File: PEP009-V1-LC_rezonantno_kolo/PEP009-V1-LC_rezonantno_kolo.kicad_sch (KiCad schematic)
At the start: 13 parts, among them J1 Screw_Terminal_01x02

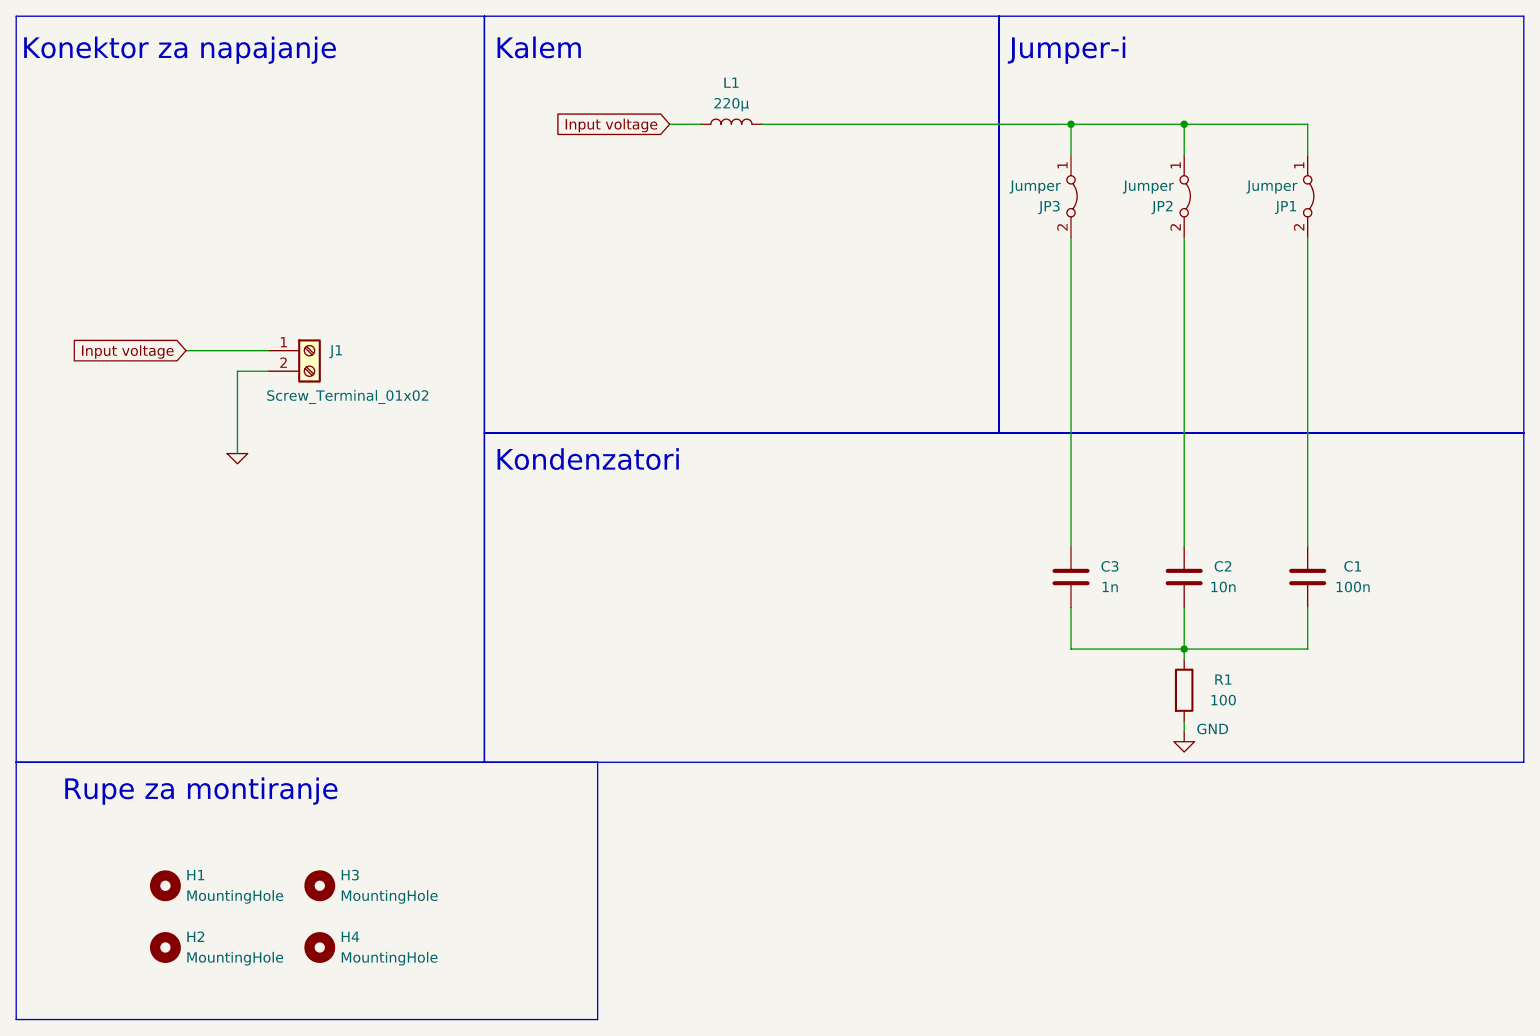
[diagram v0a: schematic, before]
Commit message: PEP006 and PEP009 update.
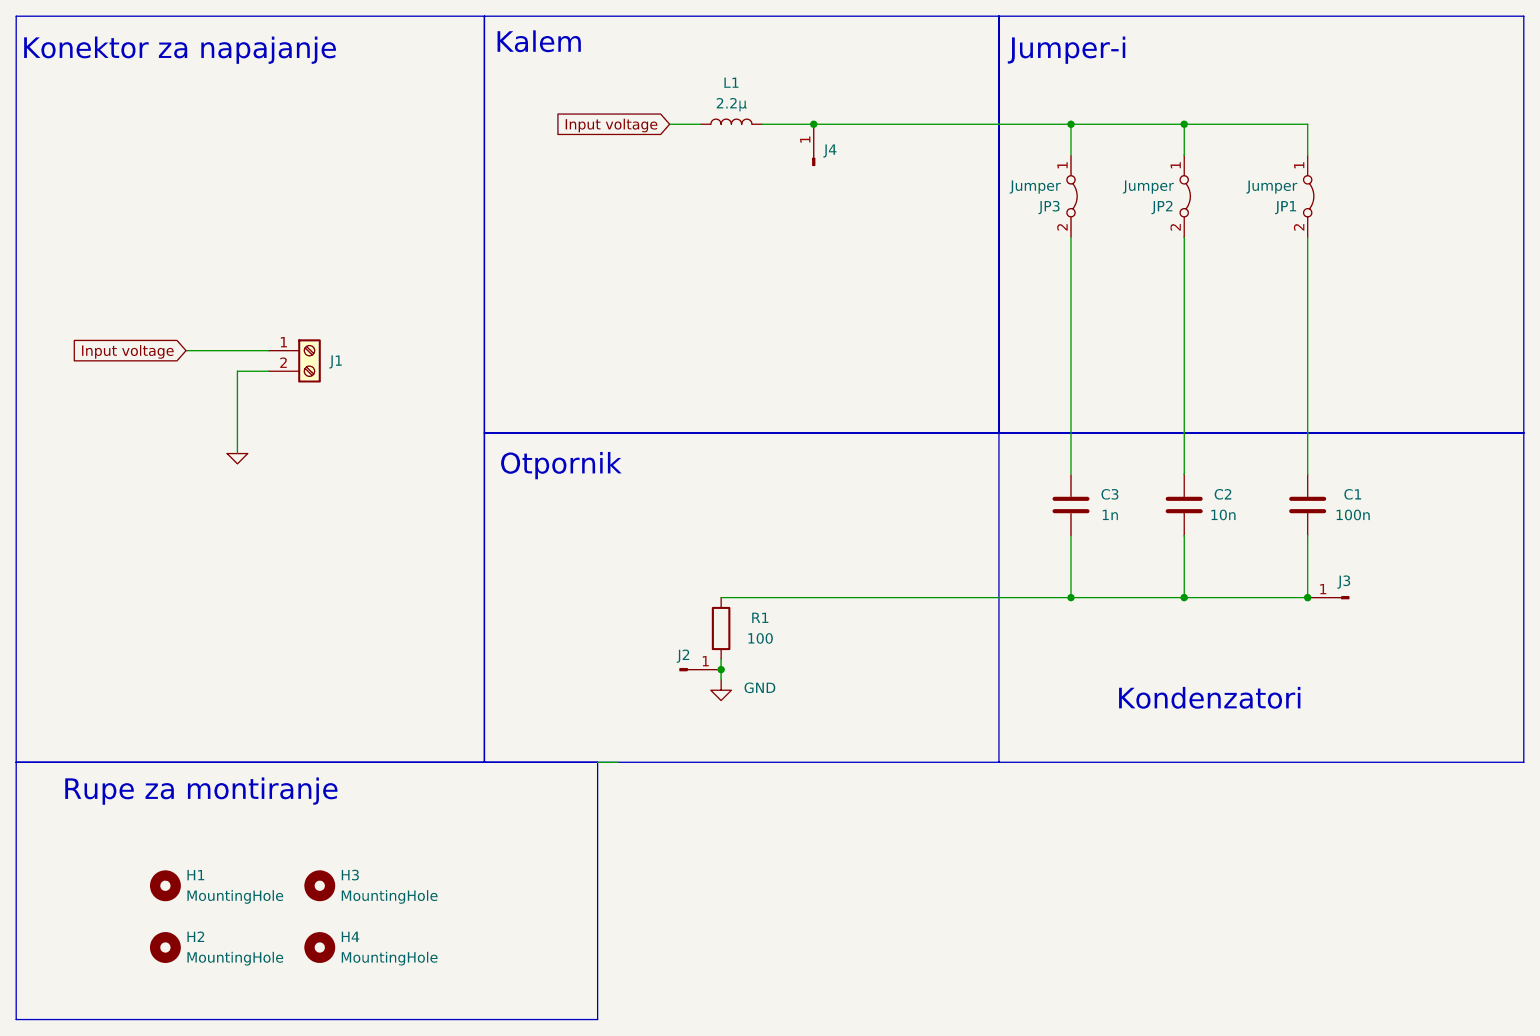
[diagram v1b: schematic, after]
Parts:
- added J2, J3, J4: Conn_01x01_Pin, Connector_PinHeader_2.54mm:PinHeader_1x01_P2.54mm_Vertical, symbol Connector:Conn_01x01_Pin
- C1: footprint Capacitor_SMD:C_1808_4520Metric -> Capacitor_SMD:C_1206_3216Metric; LCSC (none) -> C24497
- C2: footprint Capacitor_SMD:C_1808_4520Metric -> Capacitor_SMD:C_1206_3216Metric; LCSC (none) -> C1846
- C3: footprint Capacitor_SMD:C_1808_4520Metric -> Capacitor_SMD:C_1206_3216Metric; LCSC (none) -> C9196
- L1: value 220µ -> 2.2µ; footprint Inductor_SMD:L_12x12mm_H4.5mm -> Inductor_SMD:L_0805_2012Metric; LCSC (none) -> C55755
- R1: LCSC (none) -> C17901
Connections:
- net GND: now also J2.1 (Pin_1)
- net at C1.2, C2.2, C3.2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: now also J3.1 (Pin_1)
- net at JP1.1 (A), JP2.1 (A), JP3.1 (A)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: now also J4.1 (Pin_1)
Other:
- note added: "Otpornik"
- moved on the sheet: C1, C2, C3, R1

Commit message: PEP009 final commit, ready for production.
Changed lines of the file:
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@@
 	(text "Kondenzatori"
 		(exclude_from_sim no)
-		(at 147.828 98.044 0)
+		(at 134.366 102.87 0)
 		(effects
 			(font

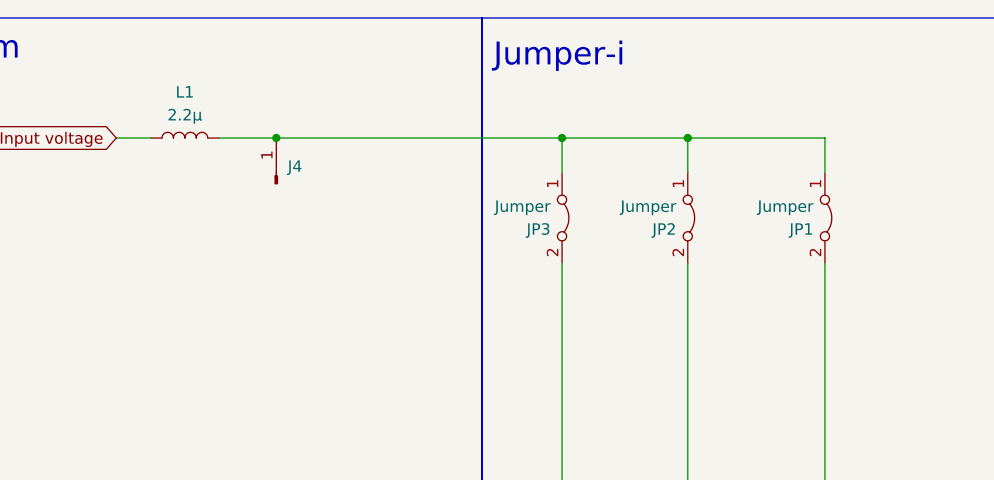
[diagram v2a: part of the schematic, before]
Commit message: Klema i kondenzatori zamenjeni sa onima iz PEP biblioteke. Naziv i broj plocice izmenjeni po standardnim pravilima
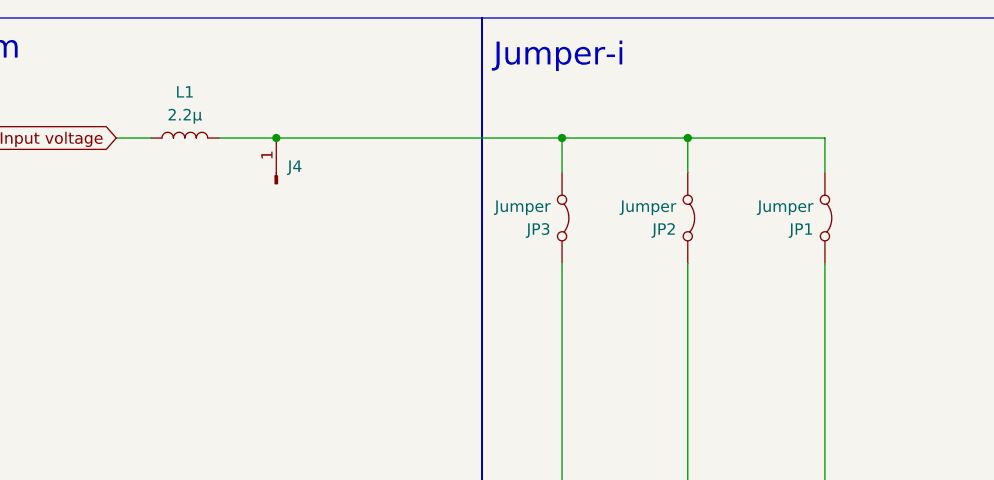
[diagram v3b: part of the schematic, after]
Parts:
- C1, C2, C3: footprint Capacitor_SMD:C_1206_3216Metric -> PEP_library:C_1206_3216Metric
- J1: footprint TerminalBlock_Phoenix:TerminalBlock_Phoenix_MKDS-1,5-2-5.08_1x02_P5.08mm_Horizontal -> PEP_library:TerminalBlock_Phoenix_MKDS-1,5-2-5.08_1x02_P5.08mm_Horizontal
- R1: footprint Resistor_SMD:R_1206_3216Metric -> PEP_library:R_smd
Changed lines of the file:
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@@
 (kicad_sch
-	(version 20231120)
+	(version 20250114)
 	(generator "eeschema")
-	(generator_version "8.0")
+	(generator_version "9.0")
 	(paper "A5")
+	(rectangle
+		(start 133.35 12.065)
+		(end 198.12 63.5)
+		(stroke
+			(width 0)
+			(type default)
+		)
+		(fill
+			(type none)
+		)
+	)
+	(rectangle
+		(start 69.85 12.065)
+		(end 133.35 63.5)
+		(stroke
+			(width 0)
+			(type default)
+		)
+		(fill
+			(type none)
+		)
+	)
+	(rectangle
+		(start 12.065 104.14)
+		(end 83.82 135.89)
+		(stroke
+			(width 0)
+			(type default)
+		)
+		(fill
+			(type none)
+		)
+	)
+	(rectangle
+		(start 69.85 63.5)
+		(end 198.12 104.14)
+		(stroke
+			(width 0)
+			(type default)
+		)
+		(fill
+			(type none)
+		)
+	)
+	(rectangle
+		(start 12.065 12.065)
+		(end 69.85 104.14)
+		(stroke
+			(width 0)
+			(type default)
+		)
+		(fill
+			(type none)
+		)
+	)
+	(text "Kondenzatori"
+		(exclude_from_sim no)
+		(at 134.366 102.87 0)
+		(effects
+			(font
+				(size 2.54 2.54)
+			)
+			(justify left bottom)
+		)
+	)
+	(text "Otpornik"
+		(exclude_from_sim no)
+		(at 79.248 67.564 0)
+		(effects
+			(font
+				(size 2.54 2.54)
+			)
+		)
+	)
+	(text "Rupe za montiranje\n"
+		(exclude_from_sim no)
+		(at 17.78 109.22 0)
+		(effects
+			(font
+				(size 2.54 2.54)
+			)
+			(justify left bottom)
+		)
+	)
+	(text "Kalem\n"
+		(exclude_from_sim no)
+		(at 71.12 17.018 0)
+		(effects
+			(font
+				(size 2.54 2.54)
+			)
+			(justify left bottom)
+		)
+	)
+	(text "Konektor za napajanje"
+		(exclude_from_sim no)
+		(at 12.7 17.78 0)
+		(effects
+			(font
+				(size 2.54 2.54)
+			)
+			(justify left bottom)
+		)
+	)
+	(text "Jumper-i"
+		(exclude_from_sim no)
+		(at 134.62 17.78 0)
+		(effects
+			(font
+				(size 2.54 2.54)
+			)
+			(justify left bottom)
+		)
+	)
 	(junction
 		(at 110.49 25.4)
@@
 			(width 0)
 			(type default)
-		)
-	)
-	(rectangle
-		(start 133.35 12.065)
-		(end 198.12 63.5)
-		(stroke
-			(width 0)
-			(type default)
-		)
-		(fill
-			(type none)
-		)
-	)
-	(rectangle
-		(start 69.85 12.065)
-		(end 133.35 63.5)
-		(stroke
-			(width 0)
-			(type default)
-		)
-		(fill
-			(type none)
-		)
-	)
-	(rectangle
-		(start 12.065 104.14)
-		(end 83.82 135.89)
-		(stroke
-			(width 0)
-			(type default)
-		)
-		(fill
-			(type none)
-		)
-	)
-	(rectangle
-		(start 69.85 63.5)
-		(end 198.12 104.14)
-		(stroke
-			(width 0)
-			(type default)
-		)
-		(fill
-			(type none)
-		)
-	)
-	(rectangle
-		(start 12.065 12.065)
-		(end 69.85 104.14)
-		(stroke
-			(width 0)
-			(type default)
-		)
-		(fill
-			(type none)
-		)
-	)
-	(text "Kondenzatori"
-		(exclude_from_sim no)
-		(at 134.366 102.87 0)
-		(effects
-			(font
-				(size 2.54 2.54)
-			)
-			(justify left bottom)
-		)
-	)
-	(text "Otpornik"
-		(exclude_from_sim no)
-		(at 79.248 67.564 0)
-		(effects
-			(font
-				(size 2.54 2.54)
-			)
-		)
-	)
-	(text "Rupe za montiranje\n"
-		(exclude_from_sim no)
-		(at 17.78 109.22 0)
-		(effects
-			(font
-				(size 2.54 2.54)
-			)
-			(justify left bottom)
-		)
-	)
-	(text "Kalem\n"
-		(exclude_from_sim no)
-		(at 71.12 17.018 0)
-		(effects
-			(font
-				(size 2.54 2.54)
-			)
-			(justify left bottom)
-		)
-	)
-	(text "Konektor za napajanje"
-		(exclude_from_sim no)
-		(at 12.7 17.78 0)
-		(effects
-			(font
-				(size 2.54 2.54)
-			)
-			(justify left bottom)
-		)
-	)
-	(text "Jumper-i"
-		(exclude_from_sim no)
-		(at 134.62 17.78 0)
-		(effects
-			(font
-				(size 2.54 2.54)
-			)
-			(justify left bottom)
 		)
 	)
@@
 			)
 		)
-		(property "Footprint" "Capacitor_SMD:C_1206_3216Metric"
+		(property "Footprint" "PEP_library:C_1206_3216Metric"
 			(at 157.1752 76.2 0)
 			(effects
@@
 			)
 		)
-		(property "Description" ""
+		(property "Description" "Jumper, 2-pole, closed/bridged"
 			(at 171.45 34.29 0)
 			(effects
@@
 			)
 		)
-		(property "Description" ""
+		(property "Description" "Mounting Hole without connection"
 			(at 49.53 127 0)
 			(effects
@@
 			)
 		)
-		(property "Footprint" "TerminalBlock_Phoenix:TerminalBlock_Phoenix_MKDS-1,5-2-5.08_1x02_P5.08mm_Horizontal"
+		(property "Footprint" "PEP_library:TerminalBlock_Phoenix_MKDS-1,5-2-5.08_1x02_P5.08mm_Horizontal"
 			(at 48.26 53.34 0)
 			(effects
@@
 			)
 		)
-		(property "Description" ""
+		(property "Description" "Generic screw terminal, single row, 01x02, script generated (kicad-library-utils/schlib/autogen/connector/)"
 			(at 48.26 53.34 0)
 			(effects
@@
 			)
 		)
-		(property "Description" ""
+		(property "Description" "Mounting Hole without connection"
 			(at 49.53 119.38 0)
 			(effects
@@
 			)
 		)
-		(property "Datasheet" "~"
+		(property "Datasheet" "https://ngspice.sourceforge.io/docs/ngspice-html-manual/manual.xhtml#subsec_Circuit_elements__device"
 			(at 39.37 66.04 0)
 			(effects
@@
 			)
 		)
-		(property "Description" ""
+		(property "Description" "0V reference potential for simulation"
 			(at 39.37 66.04 0)
 			(effects
@@
 			)
 		)
-		(property "Description" ""
+		(property "Description" "Jumper, 2-pole, closed/bridged"
 			(at 156.21 34.29 0)
 			(effects
@@
 			)
 		)
-		(property "Footprint" "Resistor_SMD:R_1206_3216Metric"
+		(property "Footprint" "PEP_library:R_smd"
 			(at 97.282 87.63 90)
 			(effects
@@
 			)
 		)
-		(property "Description" ""
+		(property "Description" "Jumper, 2-pole, closed/bridged"
 			(at 142.24 34.29 0)
 			(effects
@@
 			)
 		)
-		(property "Footprint" "Capacitor_SMD:C_1206_3216Metric"
+		(property "Footprint" "PEP_library:C_1206_3216Metric"
 			(at 172.4152 76.2 0)
 			(effects
@@
 			)
 		)
-		(property "Description" ""
+		(property "Description" "Mounting Hole without connection"
 			(at 30.48 127 0)
 			(effects
@@
 			)
 		)
-		(property "Description" ""
+		(property "Description" "Mounting Hole without connection"
 			(at 30.48 119.38 0)
 			(effects
@@
 			)
 		)
-		(property "Footprint" "Capacitor_SMD:C_1206_3216Metric"
+		(property "Footprint" "PEP_library:C_1206_3216Metric"
 			(at 143.2052 76.2 0)
 			(effects
@@
 		)
 	)
+	(embedded_fonts no)
 )
